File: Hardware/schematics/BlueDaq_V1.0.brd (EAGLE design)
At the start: 100 x 80 mm, 72 parts, among them IC1 MEGA8-AI, Q1 MMBT2222, Q2 MMBT2222, Q3 MMBT2222, Q4 MMBT2222, U1 MCP73831, U2 TPS61200, U3 BME280, U4 MIC5225-3.3, U5 MIC5219 5V, X1 USB-MICROB, X2 3.5mm, X4 3.5mm, Y1 16 mhz

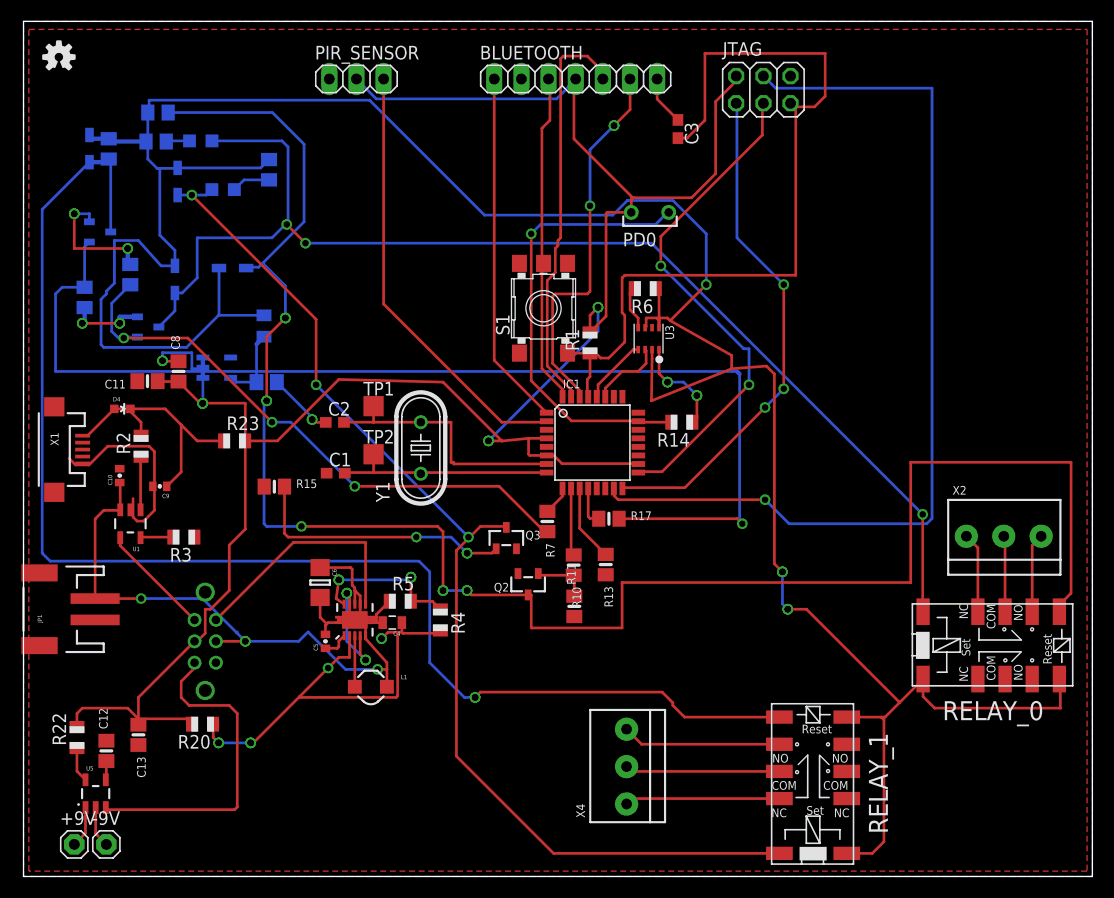
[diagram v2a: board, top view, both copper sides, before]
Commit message: removed errors
less DRC errors
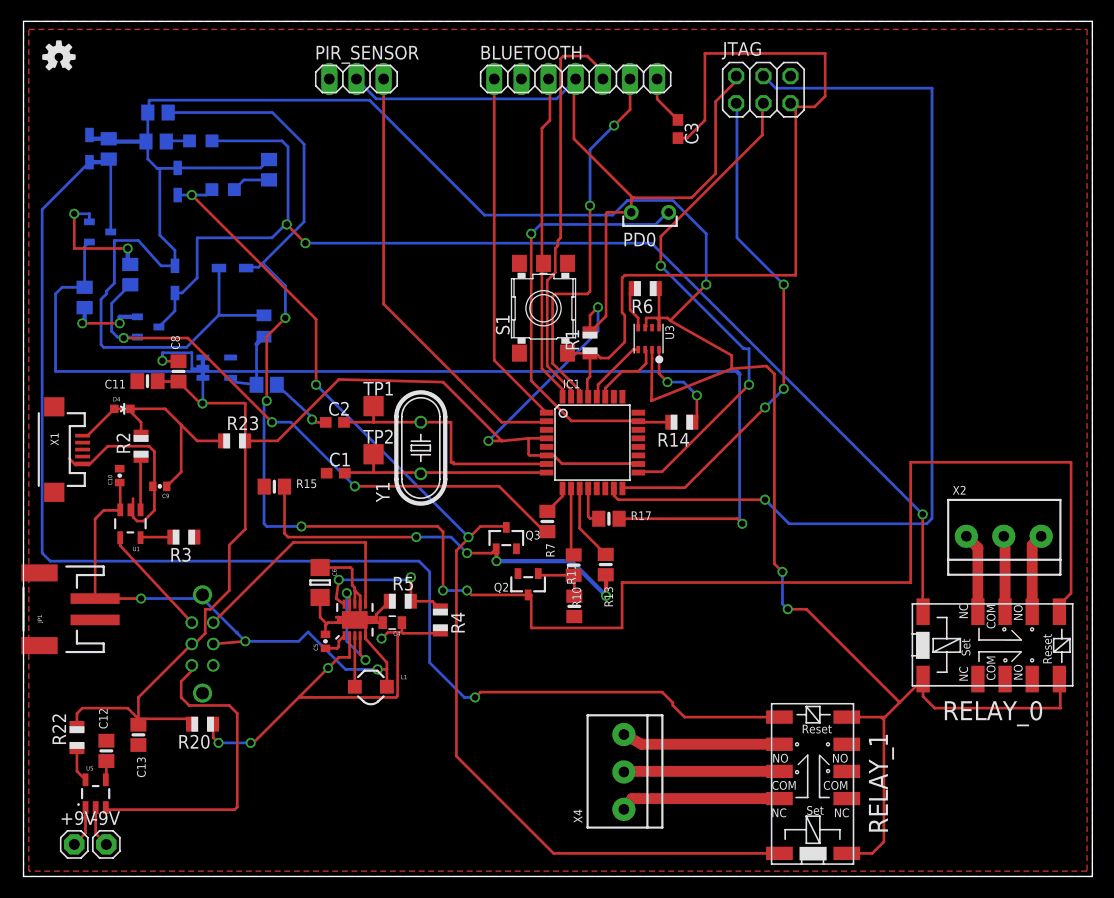
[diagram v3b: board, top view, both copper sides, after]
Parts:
- moved X4 0.56 mm to (56.2, 9.73)
- moved S2 0.35 mm to (16.8, 21.8)
- moved C7 0.25 mm to (22.8, 46.0)
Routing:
- net N$8: track 25.1 -> 39.9 mm, vias 2 -> 4
- net N$10: track 14.5 -> 15.1 mm
- net VCC: track 196.3 -> 196.2 mm, vias 4 -> 3

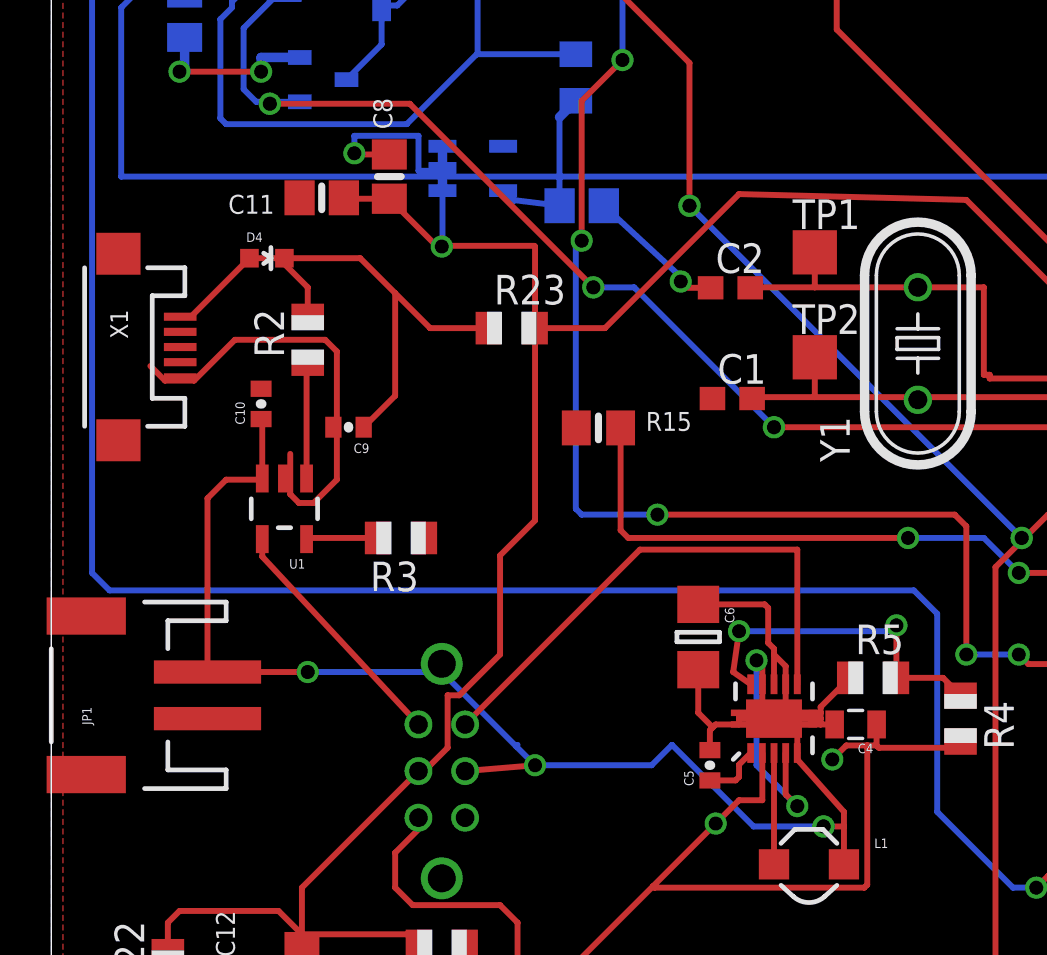
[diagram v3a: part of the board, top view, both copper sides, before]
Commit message: removed DRC errors
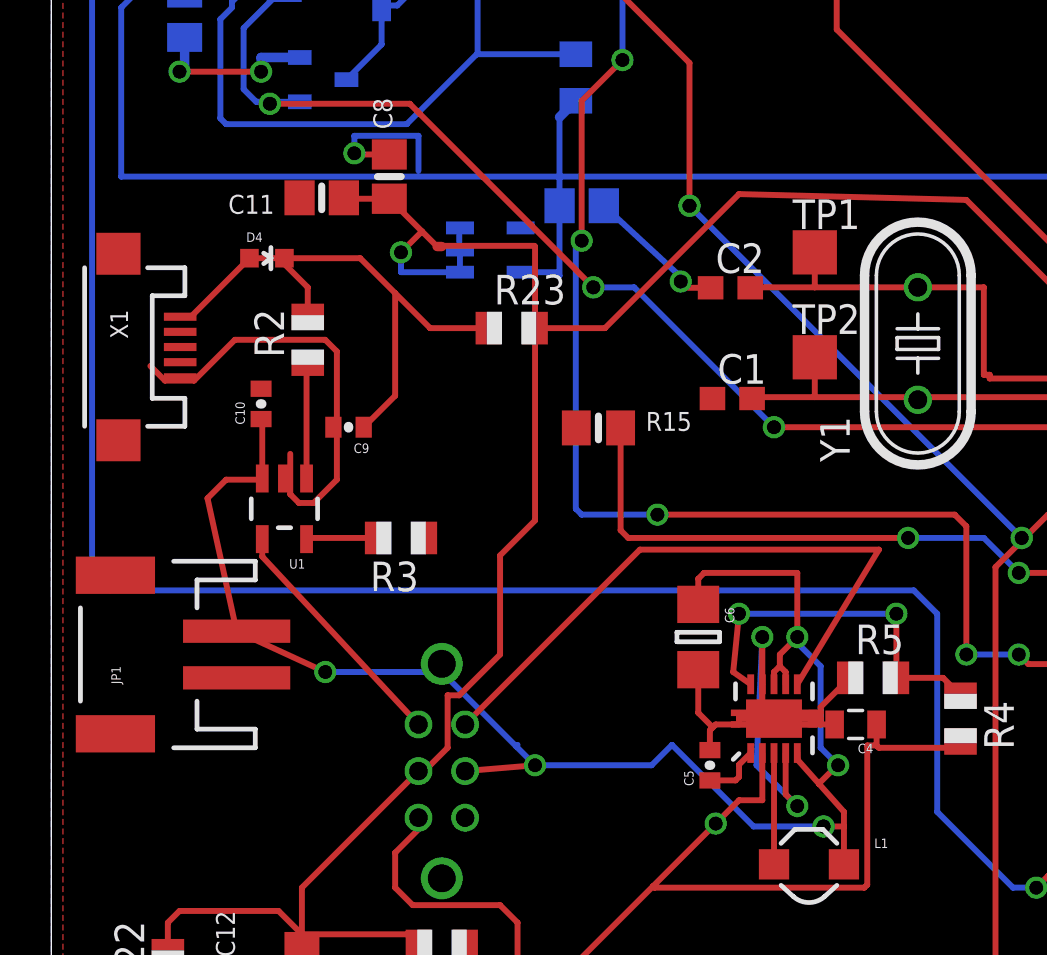
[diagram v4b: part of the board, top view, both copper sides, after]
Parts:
- moved U4 3.58 mm to (18.8, 44.1)
- moved JP1 2.15 mm to (4.25, 26.8)
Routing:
- net VBATT: track 63.2 -> 68.5 mm, vias 3 -> 5
- net EN_BC: track 23.1 -> 27.6 mm
- net VCC: track 196.2 -> 198.5 mm
- net OUT: track 7.39 -> 9.61 mm
- net PGND: track 25.5 -> 27.4 mm
- net N$20: track 41.6 -> 39.8 mm, vias 4 -> 3
- net FB: track 14.8 -> 16.0 mm
- net GND: track 61.9 -> 60.7 mm

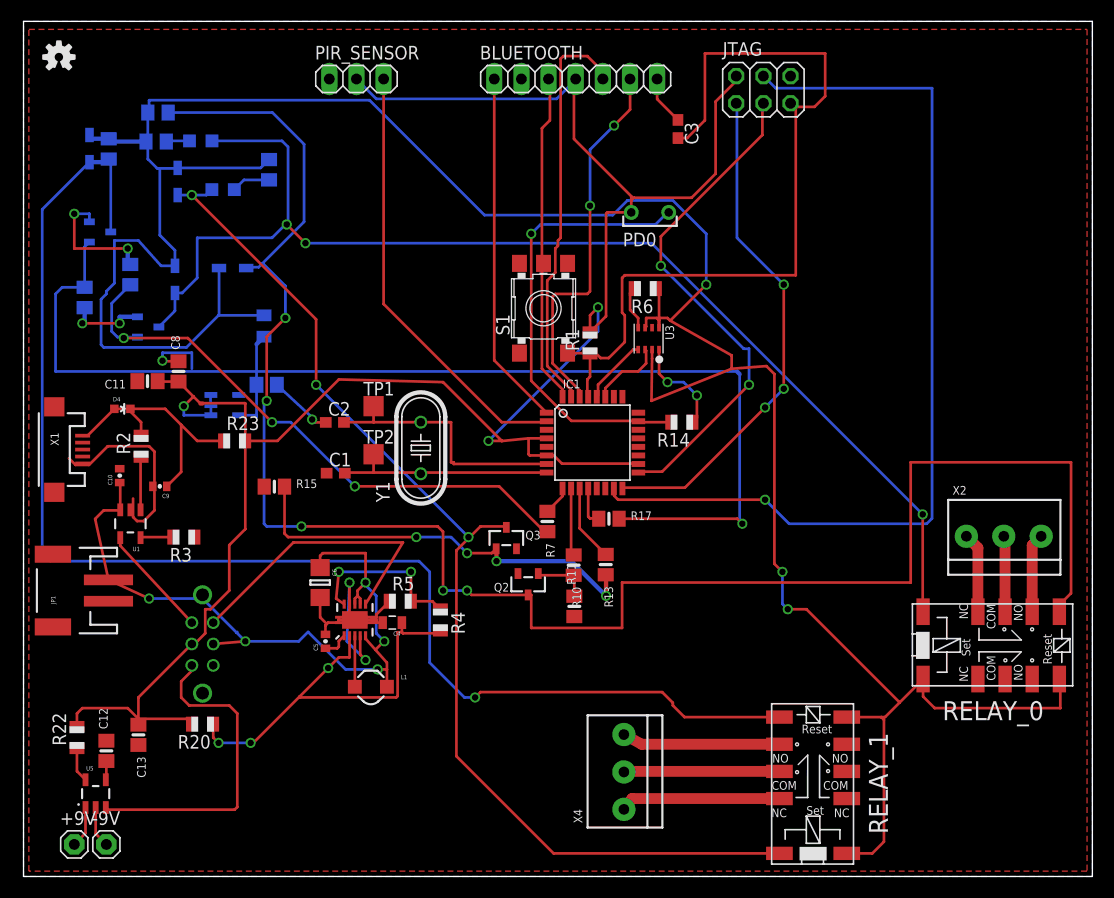
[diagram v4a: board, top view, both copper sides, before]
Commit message: removed more DRC errors
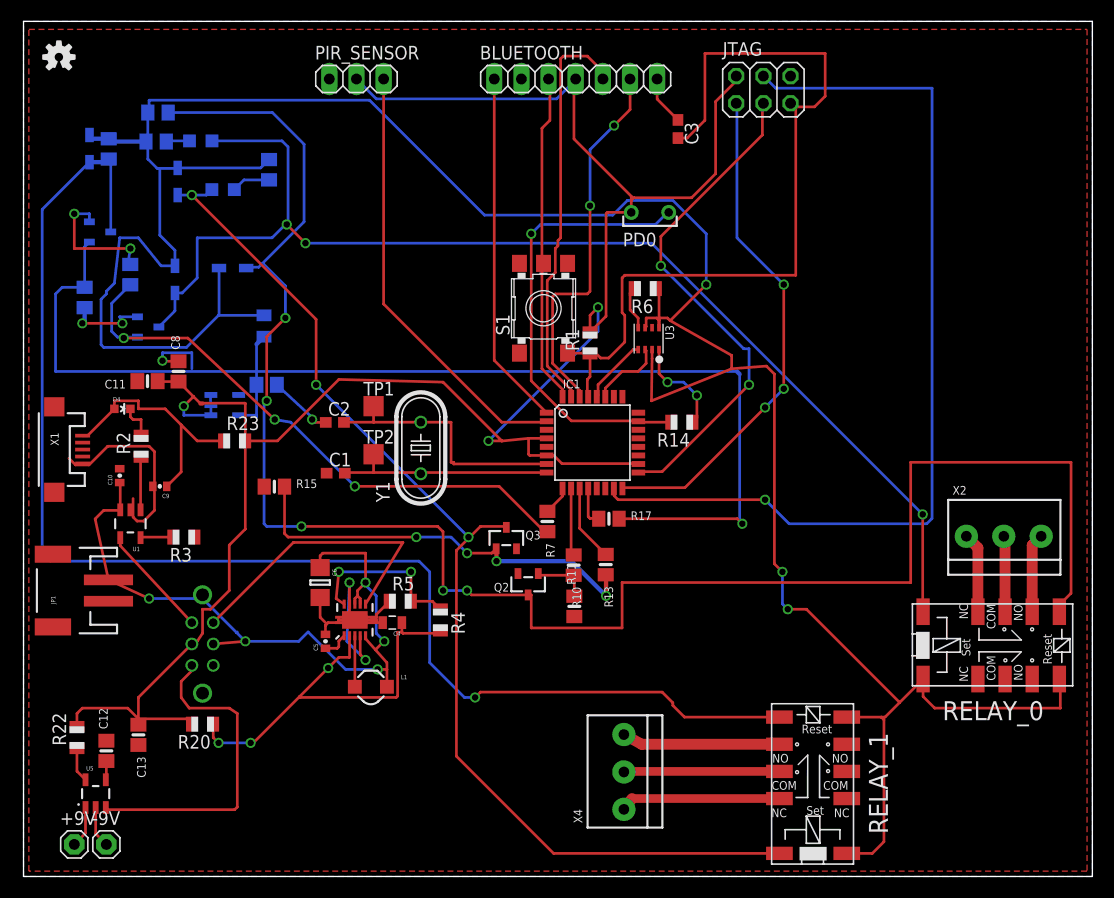
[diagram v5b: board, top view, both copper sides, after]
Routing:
- net N$23: track 21.8 -> 23.3 mm
- net GND: track 60.7 -> 61.3 mm
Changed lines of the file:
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@@
 <wire x1="20.75" y1="44.25" x2="20.75" y2="40.75" width="0.254" layer="1"/>
 <wire x1="15.75" y1="21.75" x2="16.25" y2="22" width="0.254" layer="1"/>
-<wire x1="16.25" y1="22" x2="17" y2="22.75" width="0.254" layer="1"/>
-<wire x1="17" y1="22.75" x2="17" y2="25" width="0.254" layer="1"/>
+<wire x1="16.25" y1="22" x2="16.75" y2="22.75" width="0.254" layer="1"/>
+<wire x1="16.75" y1="22.75" x2="16.75" y2="25" width="0.254" layer="1"/>
 <wire x1="10.75" y1="14.75" x2="10.75" y2="14.2" width="0.254" layer="1"/>
-<wire x1="17" y1="25" x2="17.5" y2="25" width="0.254" layer="1"/>
+<wire x1="16.75" y1="25" x2="17.5" y2="25" width="0.254" layer="1"/>
 <wire x1="17.5" y1="25" x2="19.25" y2="26.75" width="0.254" layer="1"/>
 <wire x1="19.25" y1="26.75" x2="19.25" y2="31" width="0.254" layer="1"/>
@@
 <wire x1="9" y1="38.125" x2="9.00003125" y2="38.14998125" width="0.254" layer="1"/>
 <wire x1="9.99" y1="57.26" x2="9.75" y2="57.26" width="0.4064" layer="16"/>
-<wire x1="9.75" y1="57.26" x2="9.75" y2="58.75" width="0.4064" layer="16"/>
-<wire x1="9.75" y1="58.75" x2="4.75" y2="58.75" width="0.254" layer="1"/>
+<wire x1="9.75" y1="57.26" x2="10" y2="58.75" width="0.254" layer="16"/>
+<wire x1="10" y1="58.75" x2="4.75" y2="58.75" width="0.254" layer="1"/>
 <wire x1="4.75" y1="58.75" x2="4.75" y2="62" width="0.254" layer="1"/>
 <wire x1="4.75" y1="62" x2="6.16" y2="62" width="0.254" layer="16"/>
 <wire x1="6.16" y1="62" x2="6.16" y2="61.25" width="0.254" layer="16"/>
-<wire x1="10.66" y1="52.36" x2="9" y2="52.36" width="0.4064" layer="16"/>
-<wire x1="9" y1="52.36" x2="9" y2="51.75" width="0.4064" layer="16"/>
-<wire x1="9" y1="51.75" x2="5.5" y2="51.75" width="0.254" layer="1"/>
+<wire x1="10.66" y1="52.36" x2="9" y2="52.36" width="0.254" layer="16"/>
+<wire x1="9" y1="52.36" x2="9.25" y2="51.75" width="0.254" layer="16"/>
+<wire x1="9.25" y1="51.75" x2="5.5" y2="51.75" width="0.254" layer="1"/>
 <wire x1="5.5" y1="51.75" x2="5.72" y2="51.75" width="0.4064" layer="16"/>
 <wire x1="5.72" y1="51.75" x2="5.72" y2="53.22" width="0.4064" layer="16"/>
@@
 <wire x1="63" y1="42.91" x2="62.59" y2="42.5" width="0.254" layer="1"/>
 <via x="5.5" y="51.75" extent="1-16" drill="0.6" diameter="0.254"/>
-<via x="9" y="51.75" extent="1-16" drill="0.6" diameter="0.254"/>
-<via x="9.75" y="58.75" extent="1-16" drill="0.6" diameter="0.254"/>
+<via x="9.25" y="51.75" extent="1-16" drill="0.6" diameter="0.254"/>
+<via x="10" y="58.75" extent="1-16" drill="0.6" diameter="0.254"/>
 <via x="60.25" y="46.25" extent="1-16" drill="0.6" diameter="0.254"/>
 <via x="63" y="45" extent="1-16" drill="0.6" diameter="0.254"/>
@@
 <wire x1="18.25" y1="52.5" x2="22.5" y2="52.5" width="0.254" layer="16"/>
 <wire x1="14.17" y1="57.13" x2="12.87" y2="57.13" width="0.254" layer="16"/>
-<wire x1="12.87" y1="57.13" x2="10.75" y2="59.5" width="0.254" layer="16"/>
-<wire x1="10.75" y1="59.5" x2="8.5" y2="59.5" width="0.254" layer="16"/>
-<wire x1="8.5" y1="59.5" x2="8.5" y2="55.5" width="0.254" layer="16"/>
+<wire x1="12.87" y1="57.13" x2="10.75" y2="59.75" width="0.254" layer="16"/>
+<wire x1="10.75" y1="59.75" x2="9" y2="59.75" width="0.254" layer="16"/>
+<wire x1="9" y1="59.75" x2="8.5" y2="55.5" width="0.254" layer="16"/>
 <wire x1="8.5" y1="55.5" x2="7.75" y2="54.75" width="0.254" layer="16"/>
 <wire x1="7.75" y1="54.75" x2="7.75" y2="54.5" width="0.254" layer="16"/>
@@
 <contactref element="D4" pad="C"/>
 <contactref element="R2" pad="2"/>
-<wire x1="11" y1="41.25" x2="11" y2="42.5" width="0.254" layer="1"/>
-<wire x1="11" y1="42.5" x2="10" y2="43.5" width="0.254" layer="1"/>
-<wire x1="10" y1="43.5" x2="10" y2="43.75" width="0.254" layer="1"/>
+<wire x1="11" y1="41.25" x2="11" y2="42.75" width="0.254" layer="1"/>
+<wire x1="11" y1="42.75" x2="10.25" y2="42.75" width="0.254" layer="1"/>
+<wire x1="10.25" y1="42.75" x2="10" y2="43" width="0.254" layer="1"/>
+<wire x1="10" y1="43" x2="10" y2="43.75" width="0.254" layer="1"/>
 </signal>
 <signal name="N$5">
@@
 <wire x1="31" y1="36.5" x2="44.5" y2="36.5" width="0.254" layer="1"/>
 <wire x1="25" y1="42.5" x2="31" y2="36.5" width="0.254" layer="16"/>
-<wire x1="23.25" y1="42.5" x2="25" y2="42.5" width="0.254" layer="16"/>
-<wire x1="15.375" y1="50.375" x2="23.25" y2="42.5" width="0.254" layer="1"/>
+<wire x1="23.5" y1="42.75" x2="25" y2="42.5" width="0.254" layer="16"/>
+<wire x1="15.375" y1="50.375" x2="23.5" y2="42.75" width="0.254" layer="1"/>
 <wire x1="9.375" y1="50.375" x2="15.375" y2="50.375" width="0.254" layer="1"/>
 <wire x1="49" y1="32.375" x2="49.01" y2="32.26" width="0.254" layer="1"/>
 <wire x1="9.375" y1="50.375" x2="9.375" y2="50.46" width="0.254" layer="16"/>
 <via x="31" y="36.5" extent="1-16" drill="0.6096"/>
-<via x="23.25" y="42.5" extent="1-16" drill="0.6096"/>
+<via x="23.5" y="42.75" extent="1-16" drill="0.6096"/>
 <via x="9.375" y="50.375" extent="1-16" drill="0.6096"/>
 </signal>
@@
 <contactref element="X4" pad="2"/>
 <contactref element="RELAY_1" pad="9"/>
-<wire x1="70.72" y1="9.83" x2="56.87" y2="9.83" width="1.016" layer="1"/>
+<wire x1="70.72" y1="9.83" x2="56.87" y2="9.83" width="0.8128" layer="1"/>
 <wire x1="56.87" y1="9.83" x2="56.17" y2="9.78" width="1.016" layer="1"/>
 </signal>
@@
 <contactref element="X4" pad="3"/>
 <contactref element="RELAY_1" pad="10"/>
-<wire x1="70.72" y1="7.29" x2="56.93" y2="7.29" width="1.016" layer="1"/>
+<wire x1="70.72" y1="7.29" x2="56.93" y2="7.29" width="0.8128" layer="1"/>
 <wire x1="56.93" y1="7.29" x2="56.17" y2="6.28" width="1.016" layer="1"/>
 </signal>
@@
 <wire x1="16" y1="19.5" x2="14.75" y2="18.25" width="0.254" layer="1"/>
 <wire x1="14.75" y1="18.25" x2="14.75" y2="16.75" width="0.254" layer="1"/>
-<wire x1="14.75" y1="16.75" x2="15.5" y2="16" width="0.254" layer="1"/>
-<wire x1="15.5" y1="16" x2="19.25" y2="16" width="0.254" layer="1"/>
-<wire x1="19.25" y1="16" x2="20" y2="15.25" width="0.254" layer="1"/>
+<wire x1="14.75" y1="16.75" x2="15.5" y2="15.75" width="0.254" layer="1"/>
+<wire x1="15.5" y1="15.75" x2="19.25" y2="15.75" width="0.254" layer="1"/>
+<wire x1="19.25" y1="15.75" x2="20" y2="15.25" width="0.254" layer="1"/>
 <wire x1="20" y1="15.25" x2="20" y2="6.5" width="0.254" layer="1"/>
 <wire x1="20" y1="6.5" x2="19.75" y2="6.25" width="0.254" layer="1"/>
@@
 <wire x1="8.5" y1="43.75" x2="5.99" y2="41.24" width="0.254" layer="1"/>
 <wire x1="5.99" y1="41.24" x2="5.53" y2="41.24" width="0.254" layer="1"/>
-<wire x1="8.5" y1="43.75" x2="13.25" y2="43.75" width="0.254" layer="1"/>
 <wire x1="13.25" y1="43.75" x2="14.75" y2="42.25" width="0.254" layer="1"/>
 <wire x1="14.75" y1="42.25" x2="16.25" y2="40.75" width="0.254" layer="1"/>
@@
 <wire x1="13.4" y1="36.5" x2="14.75" y2="37.85" width="0.254" layer="1"/>
 <wire x1="14.75" y1="37.85" x2="14.75" y2="42.25" width="0.254" layer="1"/>
+<wire x1="10.75" y1="44.5" x2="8.5" y2="44.5" width="0.254" layer="1"/>
+<wire x1="8.5" y1="44.5" x2="8.5" y2="43.75" width="0.254" layer="1"/>
+<wire x1="13.25" y1="43.75" x2="10.75" y2="43.75" width="0.254" layer="1"/>
+<wire x1="10.75" y1="43.75" x2="10.75" y2="44.5" width="0.254" layer="1"/>
 </signal>
 <signal name="N$38">

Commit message: no more DRC errors!
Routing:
- net GND: track 61.3 -> 74.6 mm, vias 8 -> 10
- net OUT: track 9.61 -> 19.3 mm, vias 0 -> 2
- net VBATT: track 68.5 -> 75.8 mm
- net BT_DSR: track 30.9 -> 36.0 mm, vias 0 -> 2
- net N$22: track 54.8 -> 59.4 mm
- net VCC: track 198.6 -> 201.4 mm, vias 3 -> 6
- net BT_STS: track 33.2 -> 35.5 mm
- net N$1: track 42.1 -> 43.2 mm
